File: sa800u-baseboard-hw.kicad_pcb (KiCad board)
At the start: 2 copper layers, 167 parts, among them IC2 TPS2378DDA, J1 MUSBRM1C1M0, J10 MC-HVT1-S04-G, J11 MC-HVT1-S04-G, J12 MC-HVT1-S04-G, J13 MC-HVT1-S04-G, J2 46756-1001, J3 WE_632723300011, J4 WE_632723300011, J5 WE_632723300011, J6 3-84952-0, J7 F52R-1A7H1-11020, J8 WE_68715014522, J9 2908-05WB-MG, Q1 2N7000, Q2 2N7000, Q3 2N7000, T1 749020010A, U1 RTL8111H, U10 MDT580M01001, U2 TS3USB30EDGSR, U3 LT9611, U4 TXB0104RUT, U5 TXS0102YZPR, U6 FT2232HL-REEL, U7 USB57442G, U8 SA800U-WF, U9 MAX13042EEBC+T, Y1 ECS-1618-250-BN-TR, Y2 ECS-1618-250-BN-TR

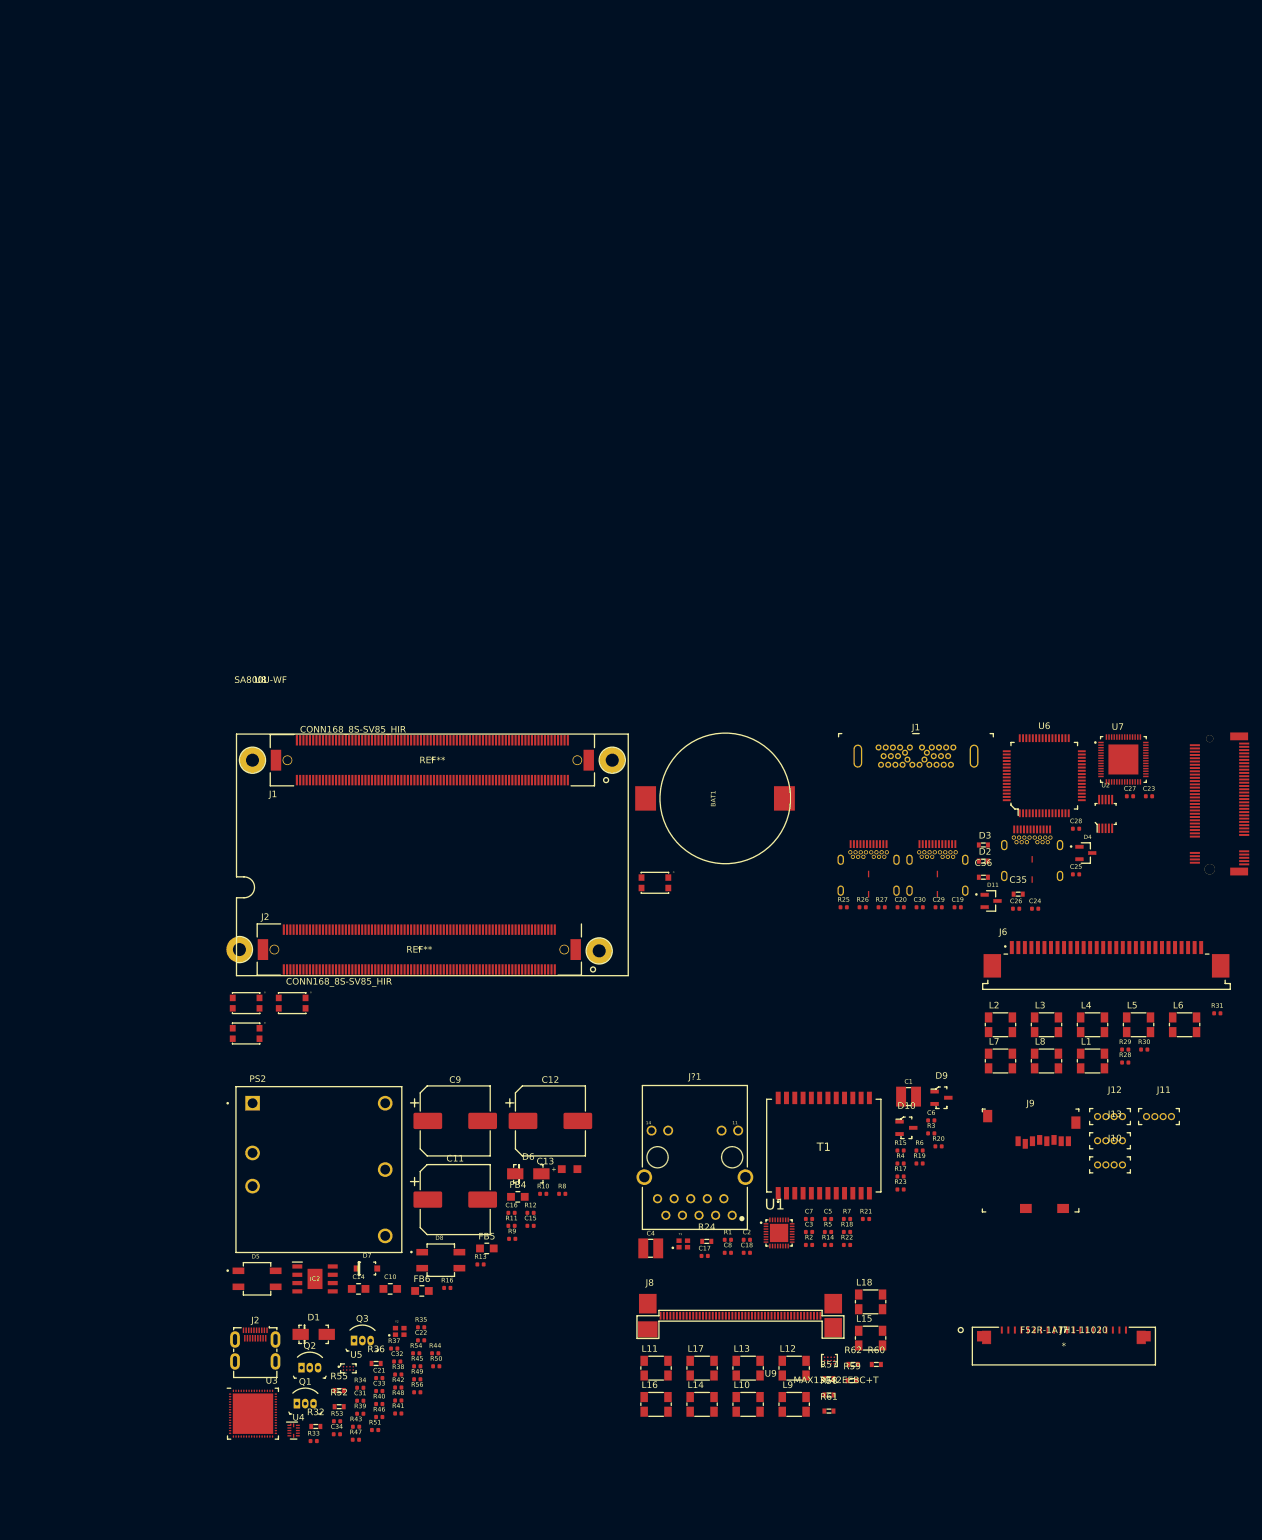
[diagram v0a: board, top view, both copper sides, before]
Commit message: added first version of board layout
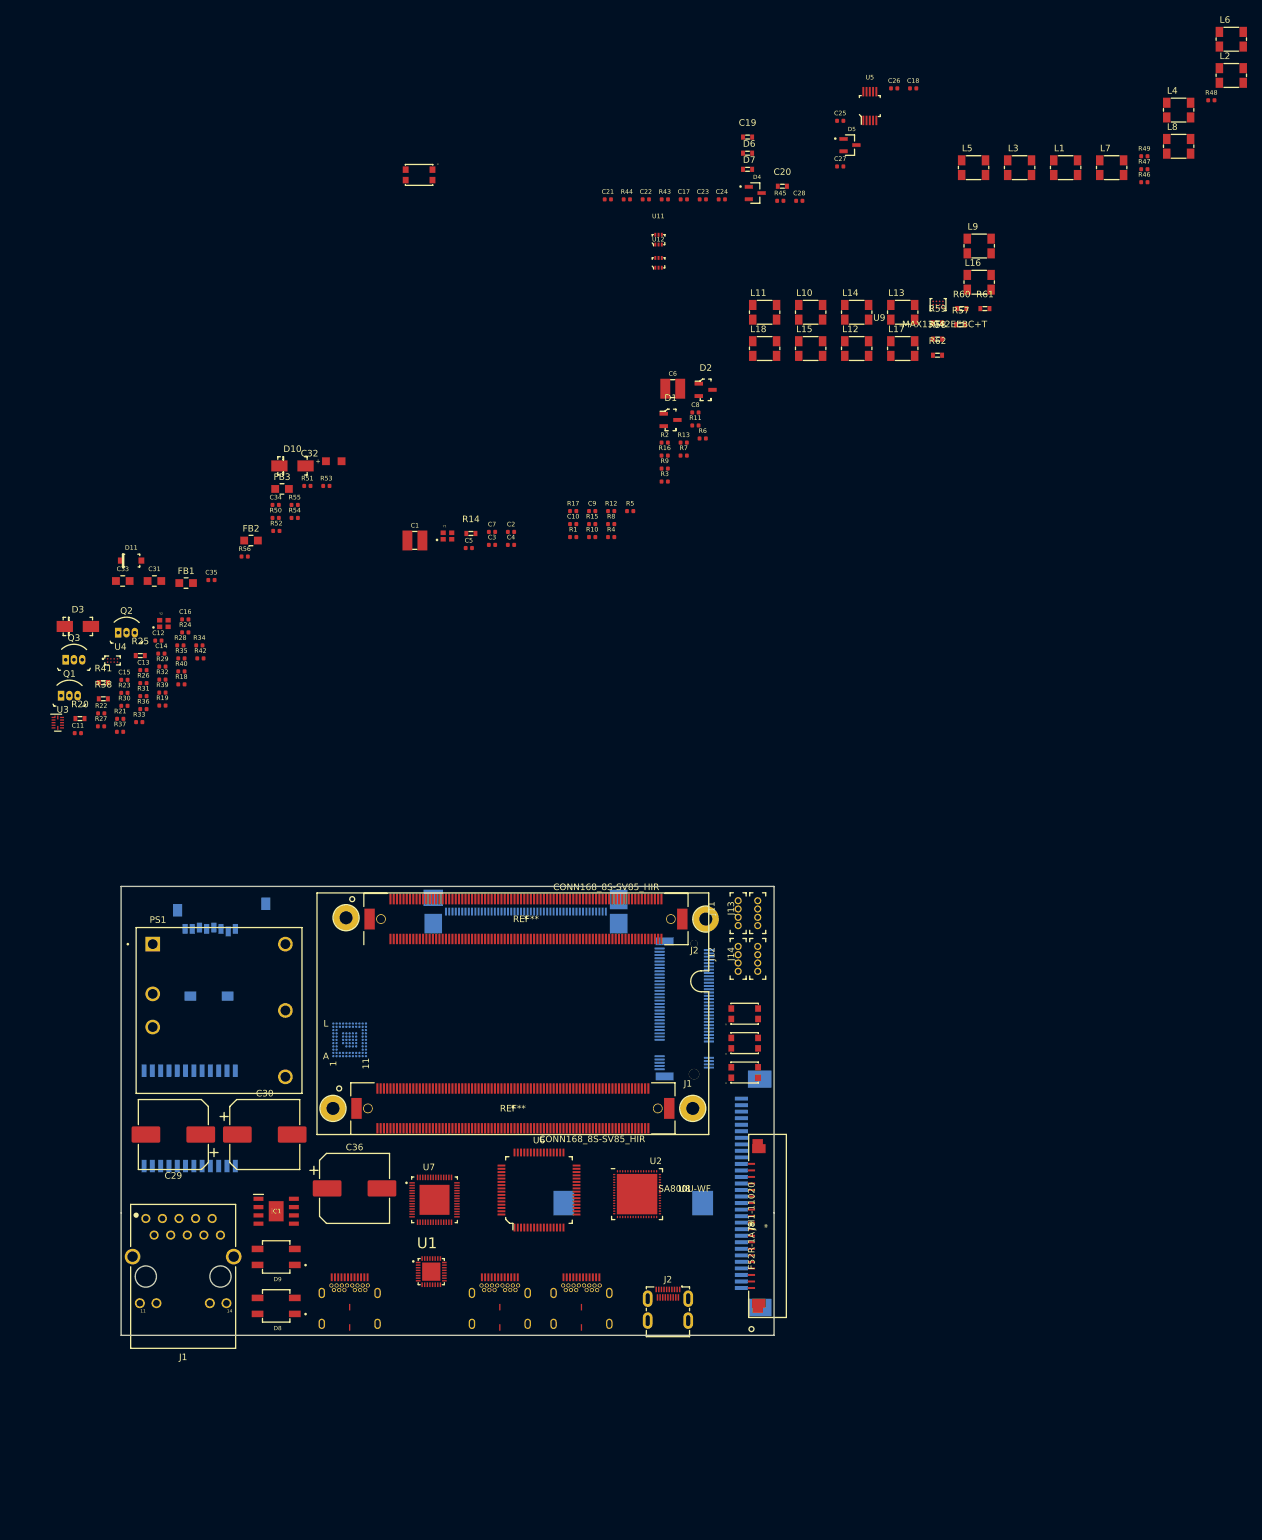
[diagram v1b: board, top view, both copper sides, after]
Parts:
- removed FB4, FB5, FB6: BLM21PG221SN1D, antmicro-footprints:0805-res
- removed IC2: TPS2378DDA, antmicro-footprints:SOIC127P600X170-9N
- removed J3: WE_632723300011, antmicro-footprints:WE_632723300011
- removed J?1: WE-RJ45_7499111121A, antmicro-footprints:7499111121A
- removed PS2: PDQE30-Q48-S5-D, antmicro-footprints:PDQE30-Q48
- added FB1: BLM21PG221SN1D, antmicro-footprints:0805-res, F.Cu at (65.0, 35.5)
- added FB2: BLM21PG221SN1D, antmicro-footprints:0805-res, F.Cu at (74.9, 29.0)
- added FB3: BLM21PG221SN1D, antmicro-footprints:0805-res, F.Cu at (79.6, 21.1)
- added IC1: TPS2378DDA, antmicro-footprints:SOIC127P600X170-9N, F.Cu at (78.8, 131.8)
- added J14: MC-HVT1-S04-G, antmicro-footprints:PinHeader_1x4_P1.27mm_Drill.7mm, F.Cu at (152.5, 95.0)
- added PS1: PDQE30-Q48-S5-D, antmicro-footprints:PDQE30-Q48, F.Cu at (70.0, 101.0)
- added U11: AP62301Z6-7, antmicro-footprints:SOT-563, F.Cu at (137.3, -17.1)
- added U12: AP62301Z6-7, antmicro-footprints:SOT-563, F.Cu at (137.3, -13.5)
- added U13: TPS65982BB, temp:TPS65982ABZBHR, B.Cu at (90.0, 105.5)
- BAT1, T1, U10: moved to B.Cu
- C10: value C_100n_0805_100V -> C_10p_0402; footprint antmicro-footprints:0805-cap -> antmicro-footprints:0402-cap
- C11: value C_47u_ELEC_100V -> C_1u_0402; footprint antmicro-footprints:CP_Elec_10x10.5 -> antmicro-footprints:0402-cap
- C12, C9: value C_47u_ELEC_100V -> C_10p_0402; footprint antmicro-footprints:CP_Elec_10x10.5 -> antmicro-footprints:0402-cap
- C13: value C_100u_KEMET_A -> C_10p_0402; footprint antmicro-footprints:KEMET_A -> antmicro-footprints:0402-cap
- C14: value C_47u_0805 -> C_100n_0402; footprint antmicro-footprints:0805-cap -> antmicro-footprints:0402-cap
- C15, C23, C28: value C_1u_0402 -> C_100n_0402
- C19, C20: value C_100n_0402 -> C_330n_0603; footprint antmicro-footprints:0402-cap -> antmicro-footprints:0603-res
- C2, C3: value C_10n_0402 -> C_100n_0402
- C21, C26, C34: value C_100n_0402 -> C_1u_0402
- C29, C30: value C_100n_0402 -> C_47u_ELEC_100V; footprint antmicro-footprints:0402-cap -> antmicro-footprints:CP_Elec_10x10.5
- C31: value C_1u_0402 -> C_100n_0805_100V; footprint antmicro-footprints:0402-cap -> antmicro-footprints:0805-cap
- C32: value C_10p_0402 -> C_100u_KEMET_A; footprint antmicro-footprints:0402-cap -> antmicro-footprints:KEMET_A
- C33: value C_10p_0402 -> C_47u_0805; footprint antmicro-footprints:0402-cap -> antmicro-footprints:0805-cap
- C35: value C_330n_0603 -> C_100n_0402; footprint antmicro-footprints:0603-res -> antmicro-footprints:0402-cap
- C36: value C_330n_0603 -> C_47u_ELEC_100V; footprint antmicro-footprints:0603-res -> antmicro-footprints:CP_Elec_10x10.5
- C4: value C_1n_1210_2kV -> C_10n_0402; footprint antmicro-footprints:1210-cap -> antmicro-footprints:0402-cap
- C6: value C_10n_0402 -> C_1n_1210_2kV; footprint antmicro-footprints:0402-cap -> antmicro-footprints:1210-cap
- C7, C8: value C_10p_0402 -> C_10n_0402
- D1: value S1G -> BZX84C6V2LT1G; footprint antmicro-footprints:DO-214AC -> antmicro-footprints:SOT-23-3
- D10: value BZX84C6V2LT1G -> SMAJ58A-13-F; footprint antmicro-footprints:SOT-23-3 -> antmicro-footprints:DO-214AC
- D11: value BZX84-C3V6,215 -> BZT52Bxx; footprint antmicro-footprints:SOT95P230X110-3N -> antmicro-footprints:SOD-123
- D2: value PGB1010603MR -> BZX84C6V2LT1G; footprint antmicro-footprints:PGB1010603MR -> antmicro-footprints:SOT-23-3
- D3: value PGB1010603MR -> S1G; footprint antmicro-footprints:PGB1010603MR -> antmicro-footprints:DO-214AC
- D5: value MB10S -> BZX84-C3V6,215; footprint antmicro-footprints:MB10S -> antmicro-footprints:SOT95P230X110-3N
- D6: value SMAJ58A-13-F -> PGB1010603MR; footprint antmicro-footprints:DO-214AC -> antmicro-footprints:PGB1010603MR
- D7: value BZT52Bxx -> PGB1010603MR; footprint antmicro-footprints:SOD-123 -> antmicro-footprints:PGB1010603MR
- D9: value BZX84C6V2LT1G -> MB10S; footprint antmicro-footprints:SOT-23-3 -> antmicro-footprints:MB10S
- J1: value MUSBRM1C1M0 -> WE-RJ45_7499111121A; footprint antmicro-footprints:USB-C_Rugged_RA_MUSBRM1C1M0 -> antmicro-footprints:7499111121A
- J10: value MC-HVT1-S04-G -> 2908-05WB-MG; footprint antmicro-footprints:PinHeader_1x4_P1.27mm_Drill.7mm -> antmicro-footprints:MicroSD_2908-05WB-MG; moved to B.Cu
- J6: value 3-84952-0 -> WE_632723300011; footprint antmicro-footprints:TE_3-84952-0 -> antmicro-footprints:WE_632723300011
- J7: value F52R-1A7H1-11020 -> 3-84952-0; footprint antmicro-footprints:F52R-1A7H1-11020 -> antmicro-footprints:TE_3-84952-0; moved to B.Cu
- J8: value WE_68715014522 -> F52R-1A7H1-11020; footprint antmicro-footprints:WE_68715014522 -> antmicro-footprints:F52R-1A7H1-11020
- J9: value 2908-05WB-MG -> WE_68715014522; footprint antmicro-footprints:MicroSD_2908-05WB-MG -> antmicro-footprints:WE_68715014522; moved to B.Cu
- R10, R13: value R_0R_0402 -> R_1k_0402
- R11: value R_100k_0402 -> R_10k_0402
- R12: value R_63R4_0402 -> R_10k_0402
- R14: value R_75R_0402 -> R_15k_0603; footprint antmicro-footprints:0402-res -> antmicro-footprints:0603-res
- R15: value R_2k49_1%_0402 -> R_470R_0402
- R16: value R_0R_0402 -> R_470R_0402
- R17: value R_470R_0402 -> R_1M0_0402
- R18: value R_470R_0402 -> R_10k_0402
- R19: value R_1M0_0402 -> R_0R_0402
- R20, R38: value R_1k_0402 -> R_10k_0603; footprint antmicro-footprints:0402-res -> antmicro-footprints:0603-res
- R21, R22: value R_10k_0402 -> R_4k7_0402
- R23: value R_1k_0402 -> R_4k7_0402
- R24: value R_15k_0603 -> R_27k_0402; footprint antmicro-footprints:0603-res -> antmicro-footprints:0402-res
- R25: value R_2k2_0402 -> R_7k68_0603; footprint antmicro-footprints:0402-res -> antmicro-footprints:0603-res
- R26: value R_100k_0402 -> R_1k_0402
- R27: value R_100k_0402 -> R_0R_0402
- R30, R31: value R_4k7_0402 -> R_2k2_0402
- R32: value R_10k_0603 -> R_20k_0402; footprint antmicro-footprints:0603-res -> antmicro-footprints:0402-res
- R33: value R_4k7_0402 -> R_0R_0402
- R36: value R_7k68_0603 -> R_1M0_0402; footprint antmicro-footprints:0603-res -> antmicro-footprints:0402-res
- R37: value R_1M0_0402 -> R_120k_0402
- R39, R43: value R_0R_0402 -> R_2k2_0402
- R41: value R_2k2_0402 -> R_10k_0603; footprint antmicro-footprints:0402-res -> antmicro-footprints:0603-res
- R42: value R_20k_0402 -> R_120k_0402
- R44: value R_10k_0402 -> R_100k_0402
- R45: value R_0R_0402 -> R_100k_0402
- R46: value R_27k_0402 -> R_4k7_0402
- R5: value R_75R_0402 -> R_2k49_1%_0402
- R50: value R_4k7_0402 -> R_63R4_0402
- R51: value R_120k_0402 -> R_24k9_0402
- R52: value R_10k_0603 -> R_0R_0402; footprint antmicro-footprints:0603-res -> antmicro-footprints:0402-res
- R53, R54: value R_2k2_0402 -> R_0R_0402
- R55: value R_10k_0603 -> R_100k_0402; footprint antmicro-footprints:0603-res -> antmicro-footprints:0402-res
- R56: value R_120k_0402 -> R_100k_0402
- R8: value R_100k_0402 -> R_75R_0402
- R9: value R_24k9_0402 -> R_75R_0402
- U2: value TS3USB30EDGSR -> LT9611; footprint antmicro-footprints:MSOP-10_W3mm -> antmicro-footprints:LT9611
- U3: value LT9611 -> TXB0104RUT; footprint antmicro-footprints:LT9611 -> antmicro-footprints:Texas_R_PUQFN-N12
- U4: value TXB0104RUT -> TXS0102YZPR; footprint antmicro-footprints:Texas_R_PUQFN-N12 -> antmicro-footprints:BGA8C50P2X4_88X188X50N
- U5: value TXS0102YZPR -> TS3USB30EDGSR; footprint antmicro-footprints:BGA8C50P2X4_88X188X50N -> antmicro-footprints:MSOP-10_W3mm
- moved R48 234.9 mm to (222.0, -38.4)
- moved R47 229.0 mm to (211.7, -27.8)
- moved R46 222.5 mm to (211.7, -25.9)
- moved R49 217.9 mm to (211.7, -29.8)
- moved U5 209.2 mm to (169.7, -37.5)
- moved D5 195.9 mm to (166.6, -31.5)
- moved R43 193.8 mm to (138.3, -23.2)
- moved R45 187.0 mm to (156.0, -23.0)
- moved C21 183.9 mm to (129.5, -23.2)
- moved C18 180.1 mm to (176.3, -40.2)
- moved L9 179.7 mm to (186.4, -16.1)
- moved R44 179.2 mm to (132.5, -23.2)
- moved L16 178.8 mm to (186.4, -10.6)
- moved D7 178.1 mm to (150.9, -27.8)
- moved C22 178.1 mm to (135.4, -23.2)
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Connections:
- C10 pad 1: /PoE/VDD -> /Ethernet_Controller/XTAL2
- C10 pad 2: Net-(C10-Pad2) -> GND
- C11 pad 1: Net-(C11-Pad1) -> RST_N
- C11 pad 2: GNDD -> GND
- C12 pad 1: Net-(C11-Pad1) -> /HDMI_converter/XTALO
- C12 pad 2: GNDD -> GND
- C13 pad 1: 5V -> /HDMI_converter/XTALI
- C14 pad 1: 5V -> 1V8
- C15 pad 1: 5V -> GND
- C15 pad 2: GND -> 3V3
- C16 pad 1: 5V -> 1V8
- C17 pad 1: PCIE1_RX_P -> Net-(C17-Pad1)
- C17 pad 2: Net-(C17-Pad2) -> /USB-C_Interface /USB1_SS_TX0_P
- C18 pad 1: PCIE1_RX_N -> Net-(C18-Pad1)
- C18 pad 2: Net-(C18-Pad2) -> /USB-C_Interface /USB1_SS_TX0_N
- C19 pad 1: Net-(C19-Pad1) -> VBUS
- C19 pad 2: /USB-C_Interface /USB1_SS_TX0_P -> /USB-C_Interface /USB1_SS_RX1_N
- C2 pad 1: PAIR78 -> PCIE1_RX_P
- C20 pad 2: /USB-C_Interface /USB1_SS_TX0_N -> /USB-C_Interface /USB1_SS_RX1_P
- C21 pad 1: 1V8 -> VBUS
- C22 pad 1: GND -> /USB-C_Interface /USB1_SS_RX0_P
- C22 pad 2: 3V3 -> Net-(C22-Pad2)
- C23 pad 1: VBUS -> /USB-C_Interface /USB1_SS_RX0_N
- C23 pad 2: GND -> Net-(C23-Pad2)
- C24 pad 1: /USB-C_Interface /USB1_SS_RX0_P -> /USB-C_Interface /USB1_SS_TX1_N
- C25 pad 1: /USB-C_Interface /USB1_SS_RX0_N -> /USB-C_Interface /USB1_SS_TX1_P
- C26 pad 1: /USB-C_Interface /USB1_SS_TX1_N -> 3V3
- C26 pad 2: Net-(C26-Pad2) -> GND
- C27 pad 1: /USB-C_Interface /USB1_SS_TX1_P -> EDP_AUX_N
- C28 pad 1: 3V3 -> EDP_AUX_P
- C28 pad 2: GND -> Net-(C28-Pad2)
- C29 pad 1: EDP_AUX_N -> Net-(C29-Pad1)
- C29 pad 2: Net-(C29-Pad2) -> GNDD
- C3 pad 1: PAIR45 -> PCIE1_RX_N
- C30 pad 1: EDP_AUX_P -> Net-(C29-Pad1)
- C30 pad 2: Net-(C30-Pad2) -> GNDD
- C31 pad 1: RST_N -> /PoE/VDD
- C31 pad 2: GND -> Net-(C31-Pad2)
- C32 pad 1: /HDMI_converter/XTALO -> 5V
- C33 pad 1: /HDMI_converter/XTALI -> 5V
- C34 pad 1: 1V8 -> 5V
- C35 pad 1: VBUS -> 5V
- C35 pad 2: /USB-C_Interface /USB1_SS_RX1_N -> GND
- C36 pad 1: Net-(C36-Pad1) -> /PoE/VDD
- C36 pad 2: /USB-C_Interface /USB1_SS_RX1_P -> Net-(C36-Pad2)
- C4 pad 1: Earth -> PAIR78
- C5 pad 1: PAIR36 -> PAIR45
- C6 pad 1: PAIR12 -> Earth
- C7 pad 1: /Ethernet_Controller/XTAL1 -> PAIR36
- C7 pad 2: GND -> Net-(C7-Pad2)
- C8 pad 1: /Ethernet_Controller/XTAL2 -> PAIR12
- C8 pad 2: GND -> Net-(C8-Pad2)
- C9 pad 1: /PoE/VDD -> /Ethernet_Controller/XTAL1
- C9 pad 2: Net-(C9-Pad2) -> GND
- D2 pad 1: /USB-C_Interface /USB_CC1 -> GND
- D2 pad 2: GND -> (no net)
- D5 pad 1: Net-(D5-Pad1) -> GND
- D5 pad 2: Net-(D5-Pad2) -> (no net)
- D5 pad 3: PAIR36 -> (no net)
- D8 pad 1: Net-(D5-Pad1) -> Net-(D8-Pad1)
- D8 pad 2: Net-(D5-Pad2) -> Net-(D8-Pad2)
- D8 pad 3: PAIR78 -> PAIR36
- D8 pad 4: PAIR45 -> PAIR12
- D9 pad 1: GND -> Net-(D8-Pad1)
- D9 pad 2: (no net) -> Net-(D8-Pad2)
- D9 pad 3: /Ethernet_Controller/ETH_LED0 -> PAIR78
- J4 pad A1: Net-(J4-PadA1) -> GND
- J4 pad A10: Net-(J4-PadA10) -> VBUS
- J4 pad A11: Net-(J4-PadA11) -> Net-(C20-Pad1)
- J4 pad A12: Net-(J4-PadA12) -> GND
- J4 pad A2: Net-(J4-PadA2) -> Net-(C17-Pad1)
- J4 pad A3: Net-(J4-PadA3) -> Net-(C18-Pad1)
- J4 pad A4: Net-(J4-PadA4) -> VBUS
- J4 pad A5: Net-(J4-PadA5) -> /USB-C_Interface /USB_CC1
- J4 pad A6: Net-(J4-PadA6) -> /USB-C_Interface /USB1_DP
- J4 pad A7: Net-(J4-PadA7) -> /USB-C_Interface /USB1_DM
- J4 pad A8: Net-(J4-PadA8) -> /USB-C_Interface /USB_SBU1
- J4 pad A9: Net-(J4-PadA9) -> VBUS
- J4 pad B1: Net-(J4-PadB1) -> GND
- J4 pad B10: Net-(J4-PadB10) -> Net-(C23-Pad2)
- J4 pad B11: Net-(J4-PadB11) -> Net-(C22-Pad2)
- J4 pad B12: Net-(J4-PadB12) -> GND
- J4 pad B2: Net-(J4-PadB2) -> Net-(C25-Pad2)
- J4 pad B3: Net-(J4-PadB3) -> Net-(C24-Pad2)
- J4 pad B4: Net-(J4-PadB4) -> VBUS
- J4 pad B5: Net-(J4-PadB5) -> /USB-C_Interface /USB_CC2
- J4 pad B6: Net-(J4-PadB6) -> /USB-C_Interface /USB1_DP
- J4 pad B7: Net-(J4-PadB7) -> /USB-C_Interface /USB1_DM
- J4 pad B8: Net-(J4-PadB8) -> /USB-C_Interface /USB_SBU2
- J4 pad B9: Net-(J4-PadB9) -> VBUS
- J7 pad 11: Net-(J7-Pad11) -> /LCM/TP_I2C_SCL
- J7 pad 12: Net-(J7-Pad12) -> /LCM/TP_I2C_SDA
- J7 pad 14: Net-(J7-Pad14) -> +3V3
- J7 pad 15: Net-(J7-Pad15) -> +3V3
- J7 pad 16: GND -> Net-(J7-Pad16)
- J7 pad 17: /LCM/TP_I2C_SCL -> Net-(J7-Pad17)
- J7 pad 18: /LCM/TP_I2C_SDA -> Net-(J7-Pad18)
- J7 pad 19: GND -> Net-(J7-Pad19)
- J7 pad 20: +3V3 -> Net-(J7-Pad20)
- J7 pad 21: (no net) -> Net-(J7-Pad21)
- J7 pad 22: (no net) -> Net-(J7-Pad22)
- J8 pad 1: /Cameras_Interface/CSI1_LN3_FFC_N -> GND
- J8 pad 10: /Cameras_Interface/CSI1_CLK_FFC_N -> GND
- J8 pad 11: /Cameras_Interface/CSI1_CLK_FFC_P -> Net-(J8-Pad11)
- J8 pad 12: GND -> Net-(J8-Pad12)
- J8 pad 13: Net-(J8-Pad13) -> GND
- J8 pad 15: GND -> Net-(J8-Pad15)
- J8 pad 16: Net-(J8-Pad16) -> GND
- J8 pad 17: Net-(J8-Pad17) -> /LCM/TP_I2C_SCL
- J8 pad 18: GND -> /LCM/TP_I2C_SDA
- J8 pad 19: /Cameras_Interface/CSI1_LN1_FFC_N -> GND
- J8 pad 2: /Cameras_Interface/CSI1_LN3_FFC_P -> Net-(J8-Pad2)
- J8 pad 20: /Cameras_Interface/CSI1_LN1_FFC_P -> +3V3
- J8 pad 21: /Cameras_Interface/CSI0_LN1_FFC_N -> (no net)
- J8 pad 22: /Cameras_Interface/CSI0_LN1_FFC_P -> (no net)
- J8 pad 3: /Cameras_Interface/CSI0_LN3_FFC_N -> Net-(J8-Pad3)
- J8 pad 4: /Cameras_Interface/CSI0_LN3_FFC_P -> GND
- J8 pad 5: /Cameras_Interface/CSI1_LN2_FFC_N -> Net-(J8-Pad5)
- J8 pad 6: /Cameras_Interface/CSI1_LN2_FFC_P -> Net-(J8-Pad6)
- J8 pad 7: /Cameras_Interface/CSI0_LN2_FFC_N -> GND
- J8 pad 8: /Cameras_Interface/CSI0_LN2_FFC_P -> Net-(J8-Pad8)
- J8 pad 9: GND -> Net-(J8-Pad9)
- J9 pad 1: Net-(J9-Pad1) -> /Cameras_Interface/CSI1_LN3_FFC_N
- J9 pad 2: Net-(J9-Pad2) -> /Cameras_Interface/CSI1_LN3_FFC_P
- J9 pad 3: Net-(J9-Pad3) -> /Cameras_Interface/CSI0_LN3_FFC_N
- J9 pad 4: Net-(J9-Pad4) -> /Cameras_Interface/CSI0_LN3_FFC_P
- J9 pad 5: Net-(J9-Pad5) -> /Cameras_Interface/CSI1_LN2_FFC_N
- J9 pad 6: Net-(J9-Pad6) -> /Cameras_Interface/CSI1_LN2_FFC_P
- J9 pad 7: Net-(J9-Pad7) -> /Cameras_Interface/CSI0_LN2_FFC_N
- J9 pad 8: Net-(J9-Pad8) -> /Cameras_Interface/CSI0_LN2_FFC_P
- J9 pad 9: Net-(J9-Pad9) -> GND
- L1 pad 2: Net-(J6-Pad2) -> Net-(J7-Pad2)
- L1 pad 3: Net-(J6-Pad3) -> Net-(J7-Pad3)
- L2 pad 2: Net-(J6-Pad5) -> Net-(J7-Pad5)
- L2 pad 3: Net-(J6-Pad6) -> Net-(J7-Pad6)
- L3 pad 2: Net-(J6-Pad8) -> Net-(J7-Pad8)
- L3 pad 3: Net-(J6-Pad9) -> Net-(J7-Pad9)
- L4 pad 2: Net-(J7-Pad2) -> Net-(J8-Pad2)
- L4 pad 3: Net-(J7-Pad3) -> Net-(J8-Pad3)
- L5 pad 2: Net-(J7-Pad5) -> Net-(J8-Pad5)
- L5 pad 3: Net-(J7-Pad6) -> Net-(J8-Pad6)
- L6 pad 2: Net-(J7-Pad8) -> Net-(J8-Pad8)
- L6 pad 3: Net-(J7-Pad9) -> Net-(J8-Pad9)
- L7 pad 2: Net-(J7-Pad11) -> Net-(J8-Pad11)
- L7 pad 3: Net-(J7-Pad12) -> Net-(J8-Pad12)
- L8 pad 2: Net-(J7-Pad14) -> Net-(J8-Pad14)
- L8 pad 3: Net-(J7-Pad15) -> Net-(J8-Pad15)
- R10 pad 1: Net-(IC2-Pad6) -> 1V8
- R10 pad 2: GNDD -> PCIE1_WAKE_N
- R11 pad 1: GNDD -> 1V8
- R11 pad 2: GNDD -> PCIE1_RST_N
- R12 pad 1: Net-(IC2-Pad3) -> 1V8
- R12 pad 2: Net-(C10-Pad2) -> PCIE1_CLKREQ_N
- R13 pad 1: Net-(PS2-Pad5) -> 3V3
- R13 pad 2: 5V -> ETH_ISOLATEB
- R14 pad 1: Net-(C6-Pad2) -> ETH_ISOLATEB
- R14 pad 2: Net-(C4-Pad2) -> GND
- R15 pad 1: GND -> Net-(J1-Pad11)
- R15 pad 2: Net-(R15-Pad2) -> 3V3
- R16 pad 1: Net-(PS2-Pad5) -> Net-(J1-Pad13)
- R16 pad 2: GND -> 3V3
- R17 pad 1: Net-(J?1-Pad11) -> /Ethernet_Controller/XTAL1
- R17 pad 2: 3V3 -> /Ethernet_Controller/XTAL2
- R18 pad 1: Net-(J?1-Pad13) -> 3V3
- R18 pad 2: 3V3 -> Net-(Q1-Pad2)
- R19 pad 1: /Ethernet_Controller/XTAL1 -> CEC_GPIO6
- R19 pad 2: /Ethernet_Controller/XTAL2 -> CEC_HDMI
- R20 pad 1: 1V8 -> 3V3
- R20 pad 2: PCIE1_WAKE_N -> RST_N
- R21 pad 1: 1V8 -> 3V3
- R21 pad 2: PCIE1_RST_N -> HDMIOUT_SCL
- R22 pad 1: 1V8 -> 3V3
- R22 pad 2: PCIE1_CLKREQ_N -> HDMIOUT_SDA
- R23 pad 2: ETH_ISOLATEB -> INTO_GPIO5
- R24 pad 1: ETH_ISOLATEB -> Net-(D3-PadK)
- R24 pad 2: GND -> CEC_HDMI
- R25 pad 1: /USB-C_Interface /SBU_SW_OE -> GND
- R25 pad 2: 1V8 -> Net-(R25-Pad2)
- R26 pad 1: Net-(C30-Pad2) -> 3V3
- R26 pad 2: GND -> I2C_ADDR
- R27 pad 1: Net-(C29-Pad2) -> I2C_ADDR
- R27 pad 2: 3v075 -> GND
- R28 pad 1: /LCM/TP_I2C_SDA -> 1V8
- R28 pad 2: +3V3 -> LT9611_GPIO5
- R29 pad 1: /LCM/TP_I2C_SCL -> 1V8
- R29 pad 2: +3V3 -> LT9611_RST
- R30 pad 1: /LCM/TP_I2C_SDA -> 5V0
- R30 pad 2: +3V3 -> SCL_HDMI
- R31 pad 1: /LCM/TP_I2C_SCL -> 5V0
- R31 pad 2: +3V3 -> SDA_HDMI
- R32 pad 1: 3V3 -> Net-(R32-Pad1)
- R32 pad 2: RST_N -> GND
- R33 pad 1: 3V3 -> Net-(R32-Pad1)
- R33 pad 2: HDMIOUT_SCL -> DETECT_HDMI
- R34 pad 2: HDMIOUT_SDA -> INTO_GPIO5
- R35 pad 2: INTO_GPIO5 -> RST_N
- R36 pad 1: GND -> /HDMI_converter/XTALO
- R36 pad 2: Net-(R36-Pad2) -> /HDMI_converter/XTALI
- R37 pad 1: /HDMI_converter/XTALO -> GND
- R37 pad 2: /HDMI_converter/XTALI -> Net-(R37-Pad2)
- R38 pad 1: 3V3 -> GND
- R38 pad 2: I2C_ADDR -> Net-(R37-Pad2)
- R39 pad 1: I2C_ADDR -> 1V8
- R39 pad 2: GND -> I2C4_SDA
- R40 pad 1: 5V0 -> 1V8
- R40 pad 2: SCL_HDMI -> I2C4_SCL
- R41 pad 1: 5V0 -> 1V8
- R41 pad 2: SDA_HDMI -> Net-(R41-Pad2)
- R42 pad 1: Net-(R42-Pad1) -> Net-(R41-Pad2)
- R43 pad 1: Net-(R42-Pad1) -> /USB-C_Interface /SBU_SW_OE
- R43 pad 2: DETECT_HDMI -> 1V8
- R44 pad 1: 3V3 -> Net-(C28-Pad2)
- R44 pad 2: Net-(Q1-Pad2) -> GND
- R45 pad 1: CEC_GPIO6 -> Net-(C27-Pad2)
- R45 pad 2: CEC_HDMI -> 3v075
- R46 pad 1: Net-(D1-PadK) -> /LCM/TP_I2C_SDA
- R46 pad 2: CEC_HDMI -> +3V3
- R47 pad 1: 1V8 -> /LCM/TP_I2C_SCL
- R47 pad 2: LT9611_GPIO5 -> +3V3
- R48 pad 1: 1V8 -> /LCM/TP_I2C_SDA
- R48 pad 2: LT9611_RST -> +3V3
- R49 pad 1: 3V3 -> /LCM/TP_I2C_SCL
- R49 pad 2: INTO_GPIO5 -> +3V3
- R5 pad 1: Net-(C2-Pad2) -> GND
- R5 pad 2: Net-(C4-Pad2) -> Net-(R5-Pad2)
- R50 pad 1: 3V3 -> Net-(IC1-Pad3)
- R50 pad 2: RST_N -> Net-(C31-Pad2)
- R51 pad 1: GND -> /PoE/VDD
- R51 pad 2: Net-(R51-Pad2) -> Net-(IC1-Pad2)
- R52 pad 1: GND -> Net-(PS1-Pad5)
- R52 pad 2: Net-(R51-Pad2) -> 5V
- R53 pad 1: 1V8 -> Net-(PS1-Pad5)
- R53 pad 2: I2C4_SDA -> GND
- R54 pad 1: 1V8 -> Net-(IC1-Pad6)
- R54 pad 2: I2C4_SCL -> GNDD
- R55 pad 1: 1V8 -> /PoE/VDD
- R55 pad 2: Net-(R55-Pad2) -> GNDD
- R56 pad 1: Net-(R55-Pad2) -> GNDD
- R56 pad 2: GND -> GNDD
- R6 pad 1: Net-(C3-Pad2) -> Net-(C4-Pad2)
- R6 pad 2: Net-(C4-Pad2) -> Net-(C6-Pad2)
- R7 pad 2: Net-(C4-Pad2) -> Net-(C6-Pad2)
- R8 pad 1: /PoE/VDD -> Net-(C7-Pad2)
- R8 pad 2: GNDD -> Net-(C6-Pad2)
- R9 pad 1: /PoE/VDD -> Net-(C8-Pad2)
- R9 pad 2: Net-(IC2-Pad2) -> Net-(C6-Pad2)
- U1 pad 17: Net-(C17-Pad2) -> Net-(C2-Pad2)
- U1 pad 18: Net-(C18-Pad2) -> Net-(C3-Pad2)
- U1 pad 31: Net-(R15-Pad2) -> Net-(R5-Pad2)
- U2 pad 1: /USB-C_Interface /SBU_SW_SEL -> Net-(U2-Pad1)
- U2 pad 10: 3V3 -> DSI1_CLK_P
- U2 pad 2: Net-(C30-Pad2) -> Net-(U2-Pad2)
- U2 pad 3: Net-(C29-Pad2) -> LT9611_VCC33_RX
- U2 pad 4: /USB-C_Interface /USB_SBU1 -> LT9611_VCC12_RX
- U2 pad 5: GND -> DSI1_LN3_N
- U2 pad 6: /USB-C_Interface /USB_SBU2 -> DSI1_LN3_P
- U2 pad 7: Net-(C30-Pad2) -> DSI1_LN2_N
- U2 pad 8: Net-(C29-Pad2) -> DSI1_LN2_P
- U2 pad 9: /USB-C_Interface /SBU_SW_OE -> DSI1_CLK_N
- U3 pad 1: Net-(U3-Pad1) -> 1V8
- U3 pad 10: DSI1_CLK_P -> I2S_WS
- U3 pad 11: DSI1_LN1_N -> 3V3
- U3 pad 12: DSI1_LN1_P -> Net-(R37-Pad2)
- U3 pad 2: Net-(U3-Pad2) -> I2S1_WS
- U3 pad 3: LT9611_VCC33_RX -> I2S1_MCLK
- U3 pad 4: LT9611_VCC12_RX -> I2S1_SCK
- U3 pad 5: DSI1_LN3_N -> I2S1_DATA0
- U3 pad 6: DSI1_LN3_P -> GND
- U3 pad 7: DSI1_LN2_N -> I2S_D0_SPDIF
- U3 pad 8: DSI1_LN2_P -> I2S_SCLK
- U3 pad 9: DSI1_CLK_N -> I2S_MCLK
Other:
- board outline added: 100 x 68.8 mm

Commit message: 2nd version of board layout
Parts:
- added REF**: mounting-hole-3mm-NPTH, antmicro-footprints:mounting-hole-3mm-NPTH, F.Cu at (152.0, 85.0)
- added REF**: mounting-hole-3mm-NPTH, antmicro-footprints:mounting-hole-3mm-NPTH, F.Cu at (152.0, 147.0)
- added REF**: mounting-hole-3mm-NPTH, antmicro-footprints:mounting-hole-3mm-NPTH, F.Cu at (58.0, 147.0)
- added REF**: mounting-hole-3mm-NPTH, antmicro-footprints:mounting-hole-3mm-NPTH, F.Cu at (58.0, 85.0)
- D8, D9, FB1, FB2, FB3, IC1: moved to B.Cu
- moved FB3 97.1 mm to (64.0, 117.0), turned to 270 degrees
- moved FB2 89.0 mm to (61.5, 117.0), turned to 270 degrees
- moved J13 85.6 mm to (67.0, 84.0), turned to 0 degrees
- moved J12 82.9 mm to (67.0, 87.0), turned to 0 degrees
- moved FB1 81.7 mm to (59.0, 117.0), turned to 90 degrees
- moved J14 79.3 mm to (74.0, 84.0), turned to 0 degrees
- moved J11 75.5 mm to (74.0, 87.0), turned to 0 degrees
- moved T1 30.1 mm to (93.0, 130.0), turned to 90 degrees
- moved C36 28.8 mm to (62.0, 126.0), turned to 270 degrees
- moved C29 26.3 mm to (86.5, 131.8), turned to 270 degrees
- moved D8 23.7 mm to (72.0, 123.5), turned to 0 degrees
- moved D9 22.3 mm to (72.0, 117.5), turned to 0 degrees
- moved IC1 19.3 mm to (61.5, 123.0)
- moved U1 13.7 mm to (105.0, 127.5)
- moved U7 12.0 mm to (102.0, 142.0)
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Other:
- board size 100 x 68.8 mm -> 100 x 68 mm

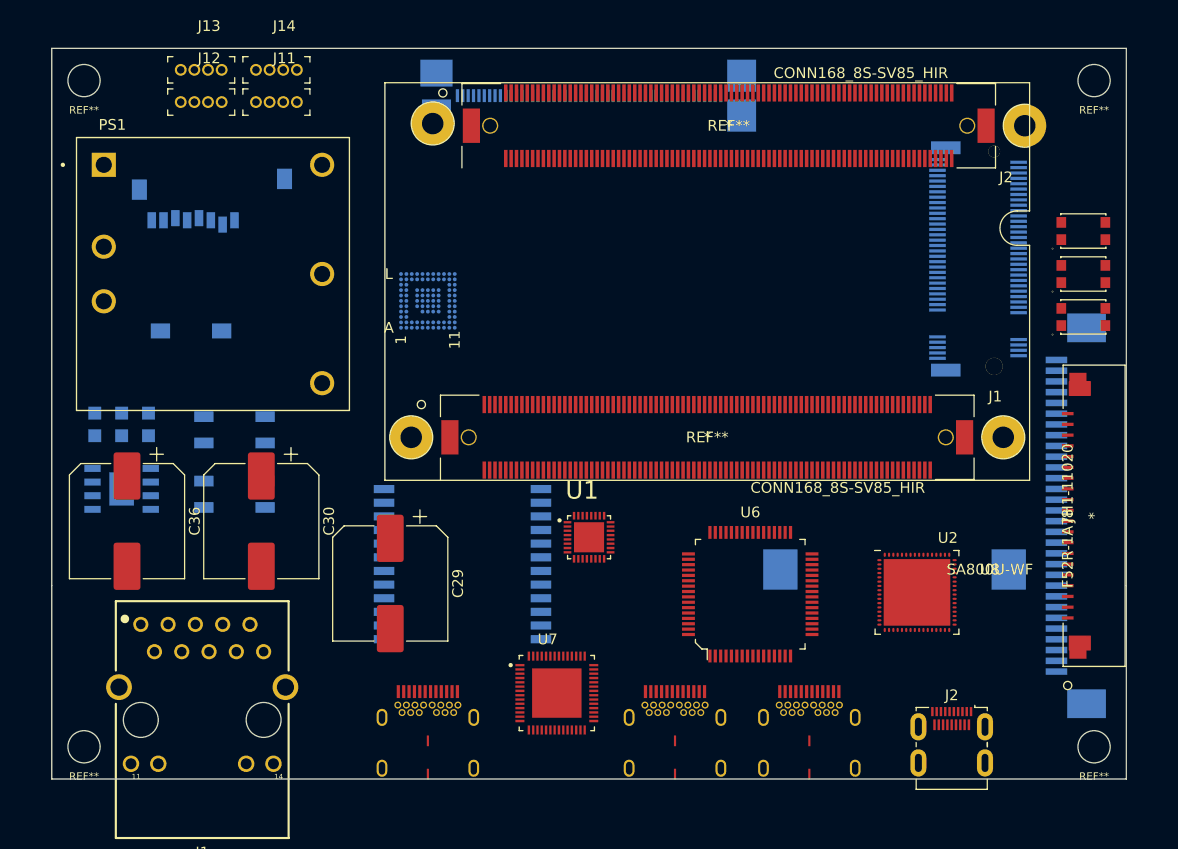
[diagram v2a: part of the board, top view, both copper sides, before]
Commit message: changed rtc battery to smaller model
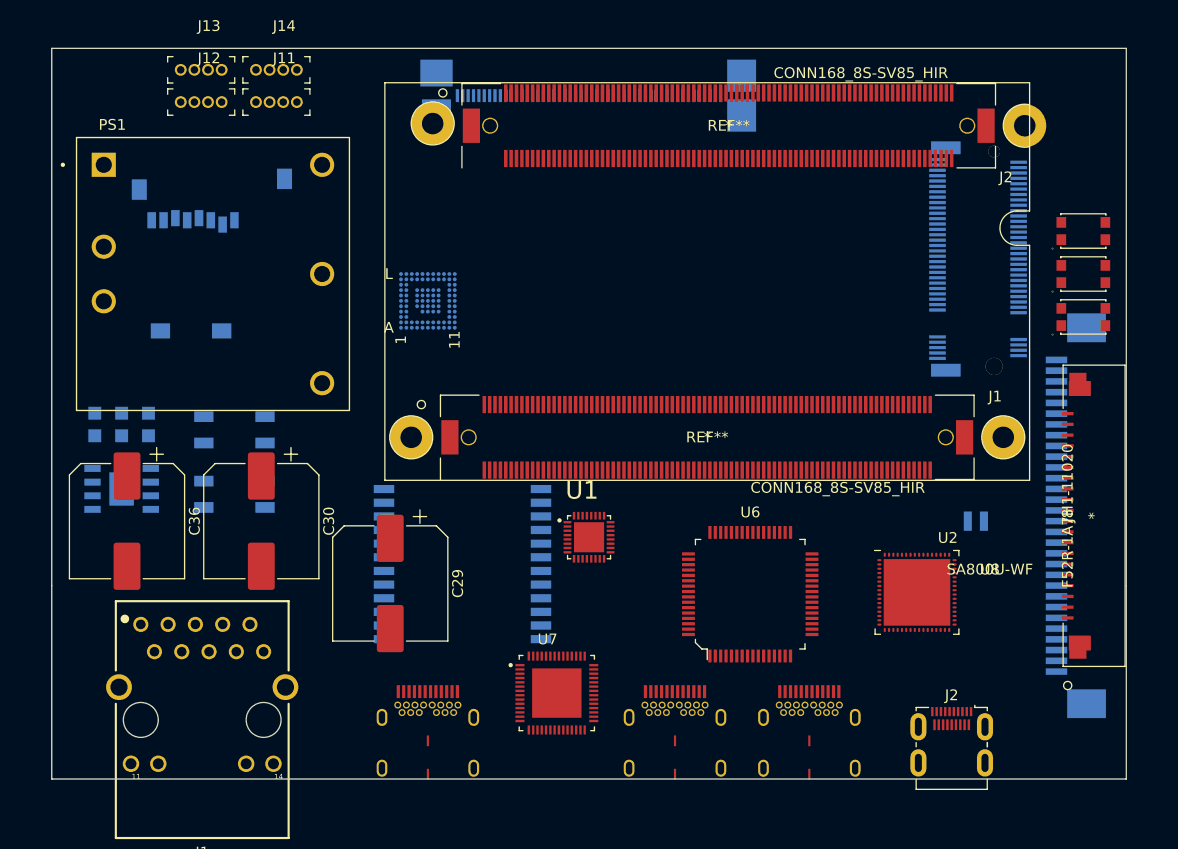
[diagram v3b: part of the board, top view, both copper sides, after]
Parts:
- removed REF** (x4): mounting-hole-3mm-NPTH, antmicro-footprints:mounting-hole-3mm-NPTH
- BAT1: value BLP2032SM-GCT-ND -> MS621FE-FL11E; footprint antmicro-footprints:BLP2032SM-GCT-ND -> antmicro-footprints:MS621FE-FL11E
- moved BAT1 7.50 mm to (141.0, 126.0)
